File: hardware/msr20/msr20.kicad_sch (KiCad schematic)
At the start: 13 parts, among them U1 RF-BPF, U2 BGA616, U3 ADE-1+, U4 AD7478, U5 Pico

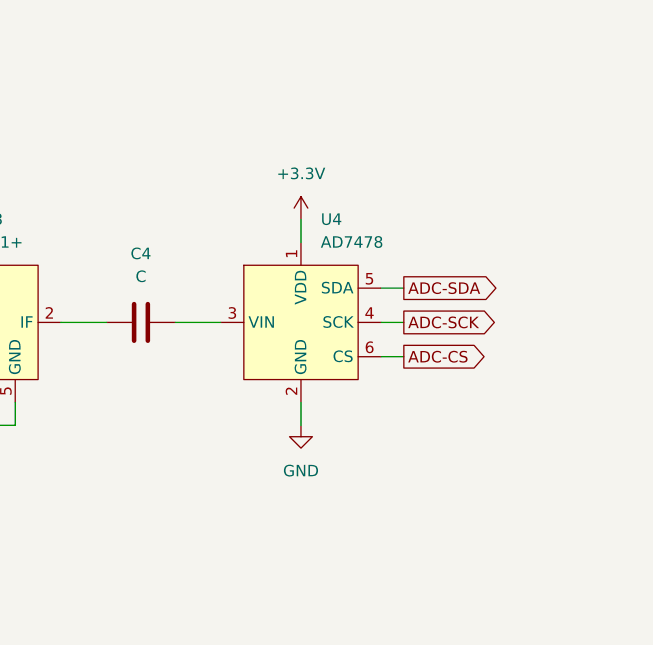
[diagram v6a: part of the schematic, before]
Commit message: update footprint assignments for passives
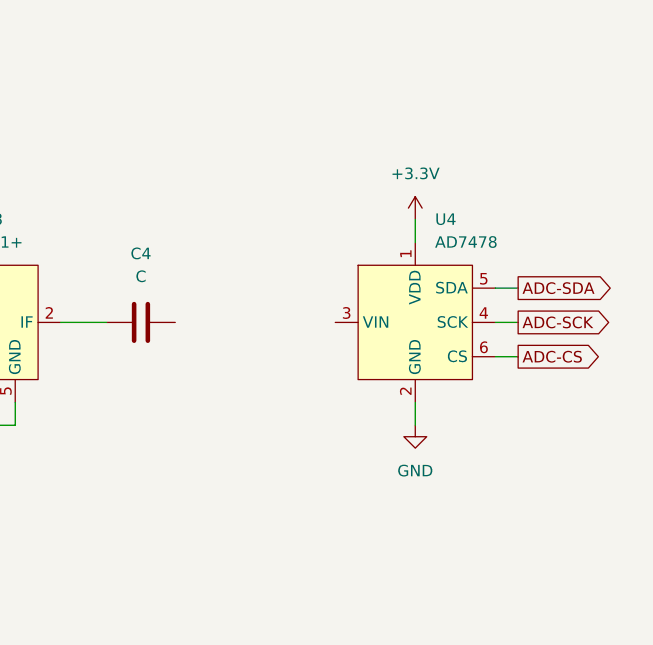
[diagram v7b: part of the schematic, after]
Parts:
- C1, C2, C3, C4: footprint (none) -> Capacitor_SMD:C_0805_2012Metric
- L1, L2: footprint (none) -> Inductor_SMD:L_0805_2012Metric
- R1: footprint (none) -> Resistor_SMD:R_0805_2012Metric
- U5: footprint RPi_Pico:RPi_Pico_SMD_TH -> MCU_RaspberryPi_and_Boards:RPi_Pico_SMD_TH
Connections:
- net at C4.2: no longer U4.3 (VIN)
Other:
- moved on the sheet: U4
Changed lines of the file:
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@@
 	(wire
 		(pts
-			(xy 204.47 63.5) (xy 207.01 63.5)
+			(xy 217.17 63.5) (xy 219.71 63.5)
 		)
 		(stroke
@@
 	(wire
 		(pts
-			(xy 204.47 71.12) (xy 207.01 71.12)
+			(xy 217.17 71.12) (xy 219.71 71.12)
 		)
 		(stroke
@@
 	(wire
 		(pts
-			(xy 195.58 55.88) (xy 195.58 58.42)
+			(xy 208.28 55.88) (xy 208.28 58.42)
 		)
 		(stroke
@@
 	(wire
 		(pts
-			(xy 195.58 76.2) (xy 195.58 78.74)
+			(xy 208.28 76.2) (xy 208.28 78.74)
 		)
 		(stroke
@@
 	(wire
 		(pts
-			(xy 204.47 67.31) (xy 207.01 67.31)
+			(xy 217.17 67.31) (xy 219.71 67.31)
 		)
 		(stroke
@@
 		(pts
 			(xy 53.34 133.35) (xy 58.42 133.35)
-		)
-		(stroke
-			(width 0)
-			(type default)
-		)
-	)
-	(wire
-		(pts
-			(xy 181.61 67.31) (xy 186.69 67.31)
 		)
 		(stroke
@@
 	(global_label "ADC-SCK"
 		(shape output)
-		(at 207.01 67.31 0)
+		(at 219.71 67.31 0)
 		(fields_autoplaced yes)
 		(effects
@@
 		)
 		(property "Intersheetrefs" "${INTERSHEET_REFS}"
-			(at 218.9457 67.31 0)
+			(at 231.6457 67.31 0)
 			(effects
 				(font
@@
 	(global_label "ADC-SDA"
 		(shape output)
-		(at 207.01 63.5 0)
+		(at 219.71 63.5 0)
 		(fields_autoplaced yes)
 		(effects
@@
 		)
 		(property "Intersheetrefs" "${INTERSHEET_REFS}"
-			(at 218.7643 63.5 0)
+			(at 231.4643 63.5 0)
 			(effects
 				(font
@@
 	(global_label "ADC-CS"
 		(shape output)
-		(at 207.01 71.12 0)
+		(at 219.71 71.12 0)
 		(fields_autoplaced yes)
 		(effects
@@
 		)
 		(property "Intersheetrefs" "${INTERSHEET_REFS}"
-			(at 217.6757 71.12 0)
+			(at 230.3757 71.12 0)
 			(effects
 				(font
@@
 			)
 		)
-		(property "Footprint" ""
+		(property "Footprint" "Capacitor_SMD:C_0805_2012Metric"
 			(at 146.05 62.5348 0)
 			(effects
@@
 			)
 		)
-		(property "Footprint" ""
+		(property "Footprint" "Capacitor_SMD:C_0805_2012Metric"
 			(at 118.11 49.8348 0)
 			(effects
@@
 			)
 		)
-		(property "Footprint" ""
+		(property "Footprint" "Resistor_SMD:R_0805_2012Metric"
 			(at 127 52.578 90)
 			(effects
@@
 			)
 		)
-		(property "Footprint" "RPi_Pico:RPi_Pico_SMD_TH"
+		(property "Footprint" "MCU_RaspberryPi_and_Boards:RPi_Pico_SMD_TH"
 			(at 76.2 152.4 90)
 			(effects
@@
 			)
 		)
-		(property "Footprint" ""
+		(property "Footprint" "Capacitor_SMD:C_0805_2012Metric"
 			(at 92.4052 73.66 0)
 			(effects
@@
 			)
 		)
-		(property "Footprint" ""
+		(property "Footprint" "Inductor_SMD:L_0805_2012Metric"
 			(at 134.62 43.18 0)
 			(effects
@@
 			)
 		)
-		(property "Footprint" ""
+		(property "Footprint" "Capacitor_SMD:C_0805_2012Metric"
 			(at 181.61 66.3448 0)
 			(effects
@@
 			)
 		)
-		(property "Footprint" ""
+		(property "Footprint" "Inductor_SMD:L_0805_2012Metric"
 			(at 99.06 63.5 0)
 			(effects
@@
 	(symbol
 		(lib_id "power:GND")
-		(at 195.58 78.74 0)
+		(at 208.28 78.74 0)
 		(unit 1)
 		(exclude_from_sim no)
@@
 		(fields_autoplaced yes)
 		(property "Reference" "#PWR08"
-			(at 195.58 85.09 0)
+			(at 208.28 85.09 0)
 			(effects
 				(font
@@
 		)
 		(property "Value" "GND"
-			(at 195.58 83.82 0)
+			(at 208.28 83.82 0)
 			(effects
 				(font
@@
 		)
 		(property "Footprint" ""
-			(at 195.58 78.74 0)
+			(at 208.28 78.74 0)
 			(effects
 				(font
@@
 		)
 		(property "Datasheet" ""
-			(at 195.58 78.74 0)
+			(at 208.28 78.74 0)
 			(effects
 				(font
@@
 		)
 		(property "Description" "Power symbol creates a global label with name \"GND\" , ground"
-			(at 195.58 78.74 0)
+			(at 208.28 78.74 0)
 			(effects
 				(font
@@
 	(symbol
 		(lib_id "power:+3.3V")
-		(at 195.58 55.88 0)
+		(at 208.28 55.88 0)
 		(unit 1)
 		(exclude_from_sim no)
@@
 		(fields_autoplaced yes)
 		(property "Reference" "#PWR07"
-			(at 195.58 59.69 0)
+			(at 208.28 59.69 0)
 			(effects
 				(font
@@
 		)
 		(property "Value" "+3.3V"
-			(at 195.58 50.8 0)
+			(at 208.28 50.8 0)
 			(effects
 				(font
@@
 		)
 		(property "Footprint" ""
-			(at 195.58 55.88 0)
+			(at 208.28 55.88 0)
 			(effects
 				(font
@@
 		)
 		(property "Datasheet" ""
-			(at 195.58 55.88 0)
+			(at 208.28 55.88 0)
 			(effects
 				(font
@@
 		)
 		(property "Description" "Power symbol creates a global label with name \"+3.3V\""
-			(at 195.58 55.88 0)
+			(at 208.28 55.88 0)
 			(effects
 				(font
@@
 	(symbol
 		(lib_id "msr20:AD7478")
-		(at 195.58 60.96 0)
+		(at 208.28 60.96 0)
 		(unit 1)
 		(exclude_from_sim no)
@@
 		(fields_autoplaced yes)
 		(property "Reference" "U4"
-			(at 197.7741 55.88 0)
+			(at 210.4741 55.88 0)
 			(effects
 				(font
@@
 		)
 		(property "Value" "AD7478"
-			(at 197.7741 58.42 0)
+			(at 210.4741 58.42 0)
 			(effects
 				(font
@@
 		)
 		(property "Footprint" "Package_TO_SOT_SMD:SOT-23-6"
-			(at 195.58 60.96 0)
+			(at 208.28 60.96 0)
 			(effects
 				(font
@@
 		)
 		(property "Datasheet" ""
-			(at 195.58 60.96 0)
+			(at 208.28 60.96 0)
 			(effects
 				(font
@@
 		)
 		(property "Description" ""
-			(at 195.58 60.96 0)
-			(effects
-				(font
+			(at 208.28 60.96 0)
+			(effects
+				(font

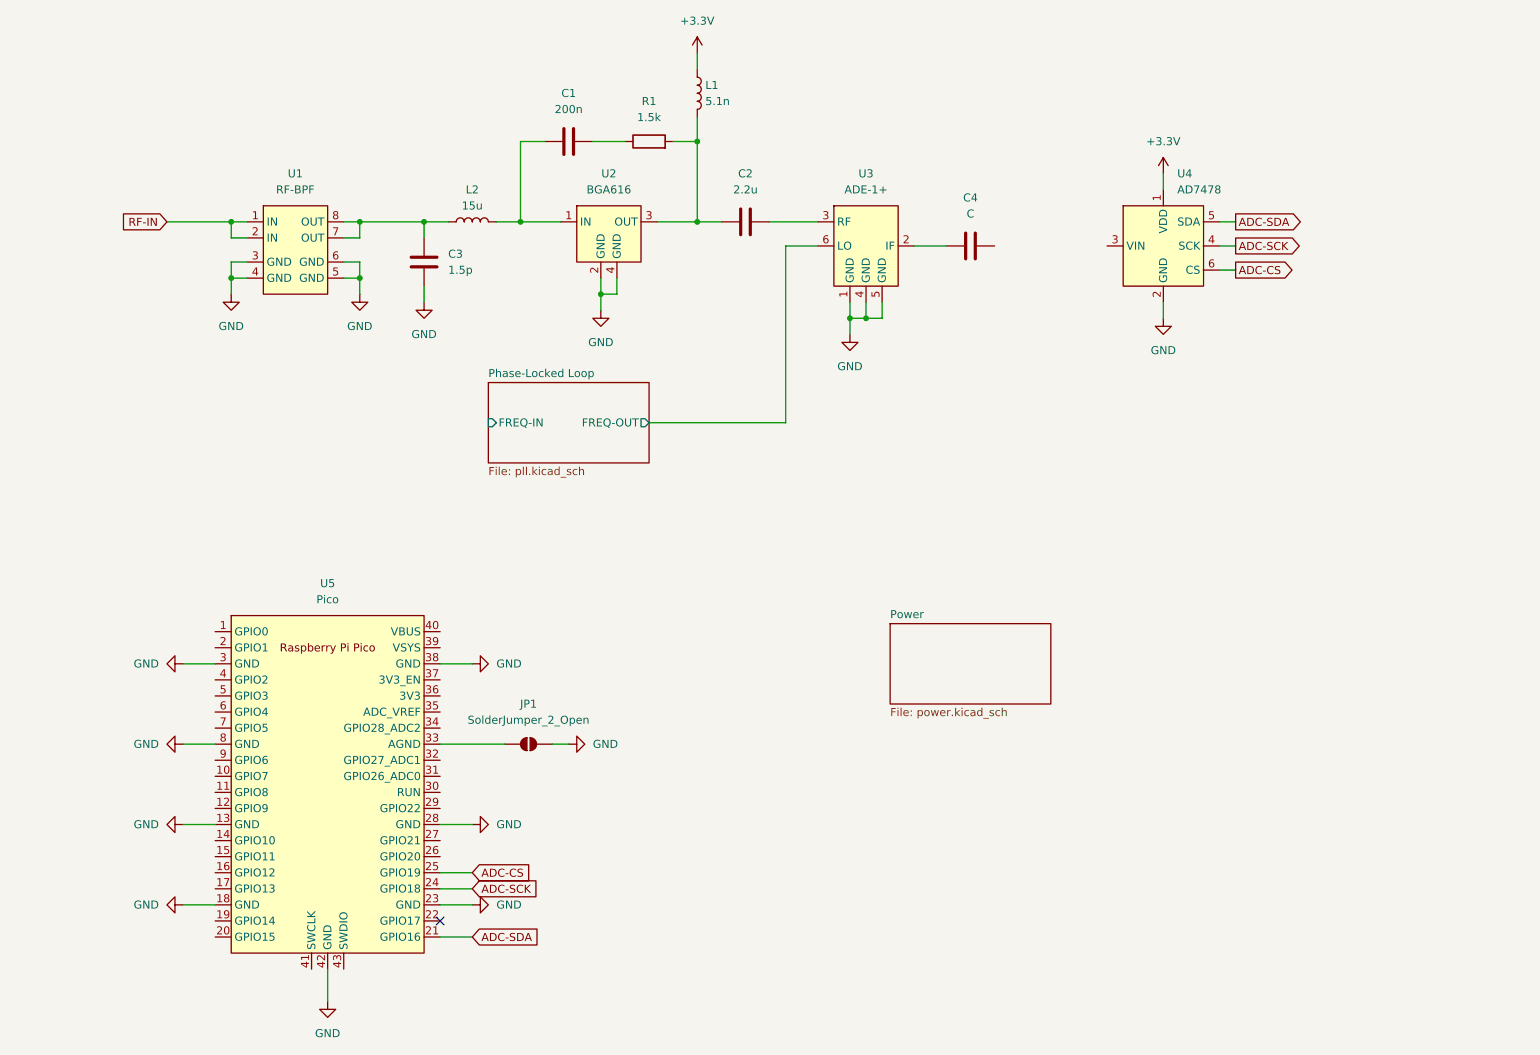
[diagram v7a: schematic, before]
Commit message: rf-bpf, lna, pll, rf mixer added to pcb
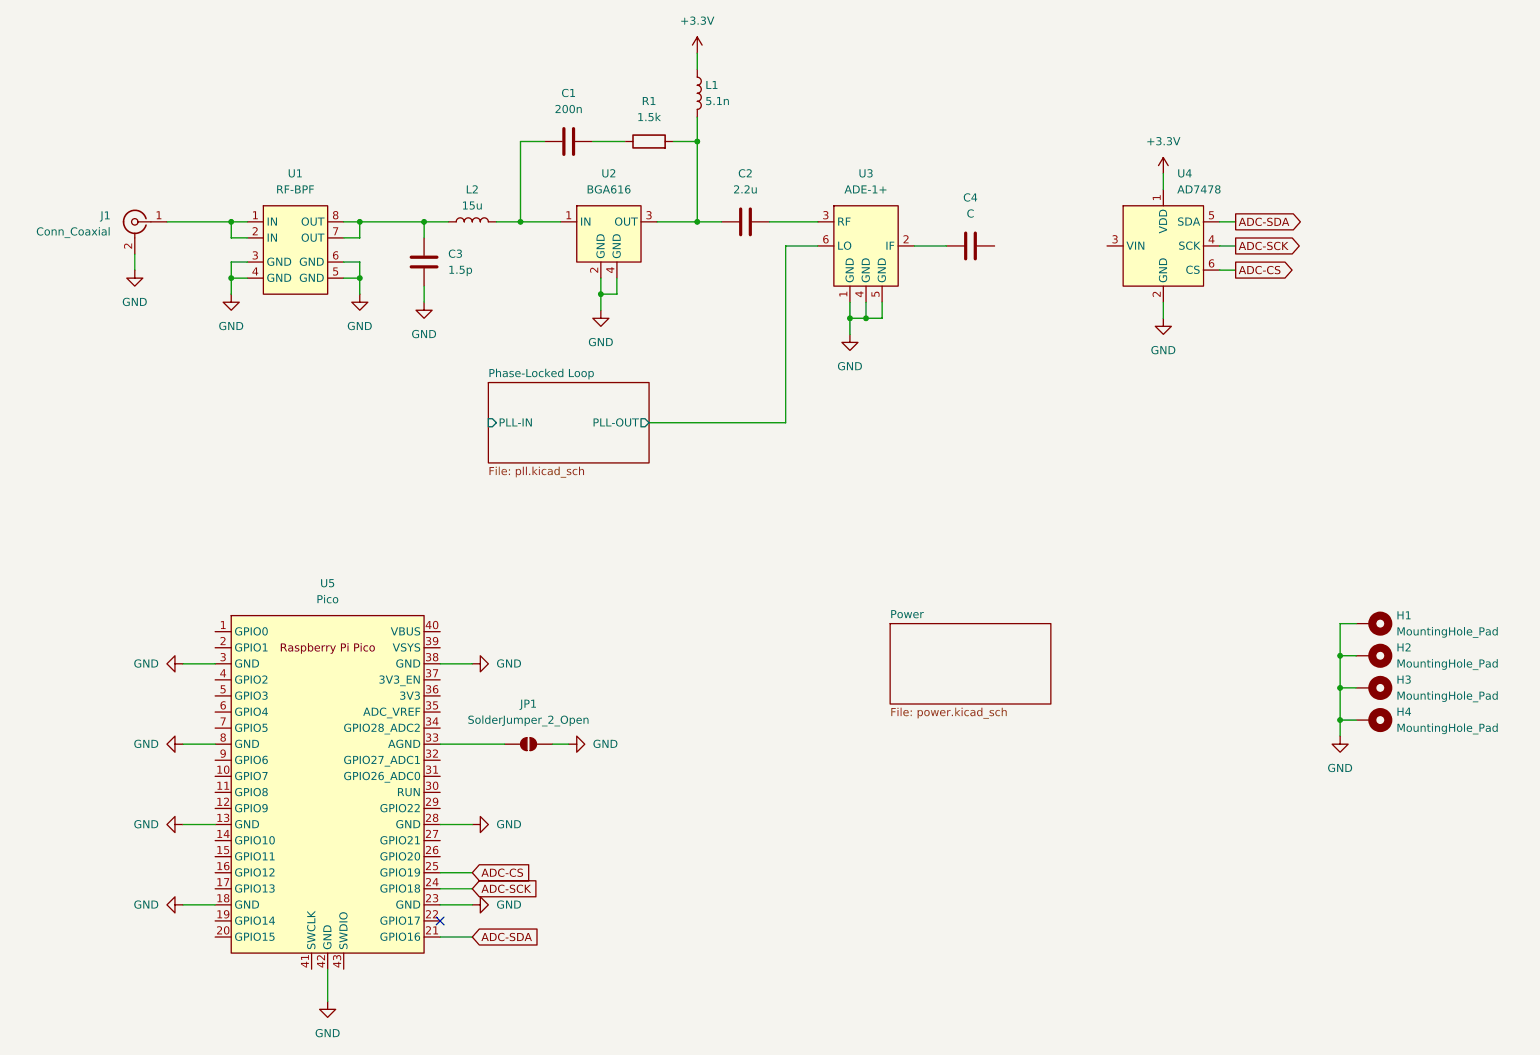
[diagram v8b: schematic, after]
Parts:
- added H1, H2, H3, H4: MountingHole_Pad, MountingHole:MountingHole_3.2mm_M3_DIN965_Pad, symbol Mechanical:MountingHole_Pad
- added J1: Conn_Coaxial, Connector_Coaxial:BNC_Amphenol_B6252HB-NPP3G-50_Horizontal, symbol Connector:Conn_Coaxial
- JP1: footprint (none) -> Jumper:SolderJumper-2_P1.3mm_Bridged2Bar_Pad1.0x1.5mm
- U3: footprint msr20:ADE-1+ -> RF_Mini-Circuits:Mini-Circuits_CD636_H4.11mm
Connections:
- net GND: now also H1.1, H2.1, H3.1, H4.1, J1.2 (Ext)
- net Phase-Locked Loop/FREQ-OUT renamed Phase-Locked Loop/PLL-OUT
- net RF-IN: no longer names the net of U1.1 (IN), U1.2 (IN)
- net RF-IN: now also J1.1 (In)
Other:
- sheet Phase-Locked Loop ports: added PLL-IN, PLL-OUT; removed FREQ-IN, FREQ-OUT
